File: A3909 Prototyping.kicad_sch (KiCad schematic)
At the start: 0 parts

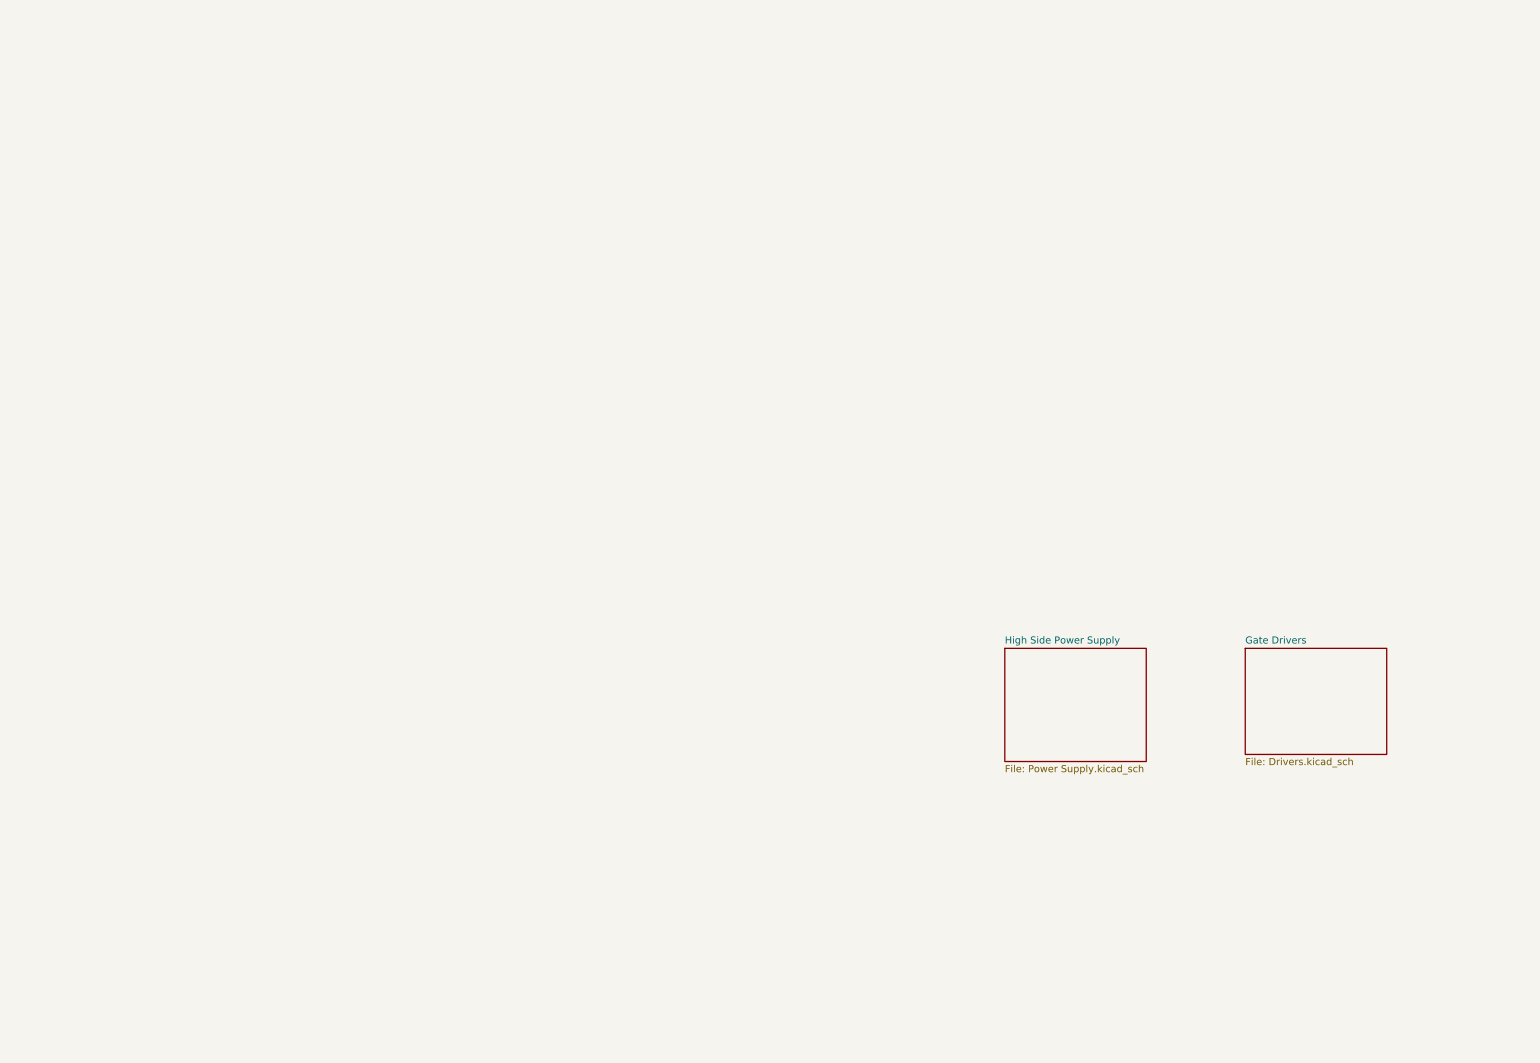
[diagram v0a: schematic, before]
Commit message: Final design Rev 1.0
Finalized design rev 1.0. Ordered from JLCPB
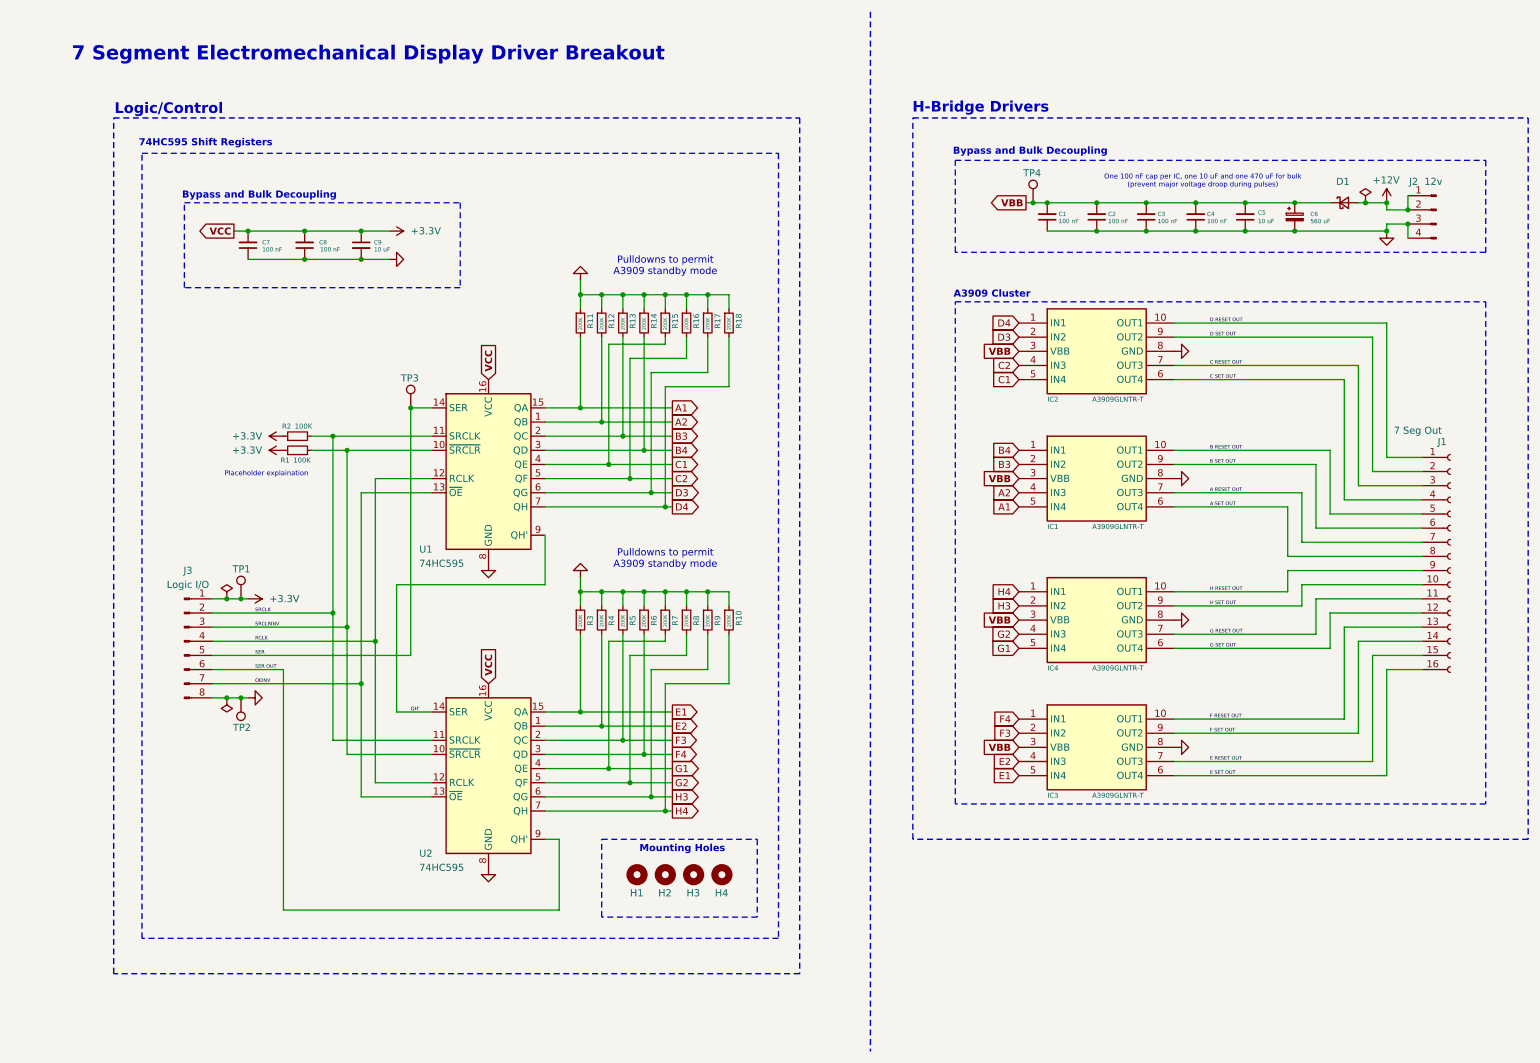
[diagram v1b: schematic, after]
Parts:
- added C1, C2, C3, C4, C7, C8: 100 nF, Capacitor_SMD:C_0402_1005Metric, symbol Device:C_Small
- added C5, C9: 10 uF, Capacitor_SMD:C_1206_3216Metric, symbol Device:C_Small
- added C6: 560 uF, Capacitor_SMD:C_Elec_10x10.2, symbol Device:C_Polarized_Small
- added D1: D_Schottky_Small, Diode_SMD:D_SMB, symbol Device:D_Schottky_Small
- added H1, H2, H3, H4: MountingHole, MountingHole:MountingHole_2.2mm_M2, symbol Mechanical:MountingHole
- added IC1, IC2, IC3, IC4: A3909GLNTR-T, KiCad:SOP100P600X175-10N, symbol A3909GLNTR-T:A3909GLNTR-T
- added J1: 7 Seg Out, Connector_PinHeader_2.54mm:PinHeader_1x16_P2.54mm_Vertical, symbol Connector:Conn_01x16_Socket
- added J2: 12v, Connector_PinHeader_2.54mm:PinHeader_1x04_P2.54mm_Vertical, symbol Connector:Conn_01x04_Pin
- added J3: Logic I/O, Connector_PinHeader_2.54mm:PinHeader_1x08_P2.54mm_Vertical, symbol Connector:Conn_01x08_Pin
- added R1, R2: 100K, Resistor_SMD:R_0402_1005Metric, symbol Device:R_Small
- added R10, R11, R12, R13, R14, R15, R16, R17, R18, R3, R4, R5, R6, R7, R8, R9: 200K, Resistor_SMD:R_0402_1005Metric, symbol Device:R_Small
- added TP1: 3.3v, TestPoint:TestPoint_Pad_D1.5mm, symbol Connector:TestPoint
- added TP2: GND, TestPoint:TestPoint_Pad_D1.5mm, symbol Connector:TestPoint
- added TP3: SER, TestPoint:TestPoint_Pad_D1.5mm, symbol Connector:TestPoint
- added TP4: 12v, TestPoint:TestPoint_Pad_D1.5mm, symbol Connector:TestPoint
- added U1, U2: 74HC595, Package_SO:SOIC-16_3.9x9.9mm_P1.27mm, symbol 74xx:74HC595
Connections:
- new net +12V: D1.2 (A), J2.1 (Pin_1), J2.2 (Pin_2)
- new net +3.3V: C7.2, C8.2, C9.1, J3.1 (Pin_1), R1.1, R2.1, TP1.1, U1.16 (VCC), U2.16 (VCC)
- new net A RESET OUT: IC1.7 (OUT3), J1.7 (Pin_7)
- new net A SET OUT: IC1.6 (OUT4), J1.8 (Pin_8)
- new net A1: IC1.5 (IN4), R11.2, U1.15 (QA)
- new net A2: IC1.4 (IN3), R12.2, U1.1 (QB)
- new net B RESET OUT: IC1.10 (OUT1), J1.5 (Pin_5)
- new net B SET OUT: IC1.9 (OUT2), J1.6 (Pin_6)
- new net B3: IC1.2 (IN2), R13.2, U1.2 (QC)
- new net B4: IC1.1 (IN1), R14.2, U1.3 (QD)
- new net C RESET OUT: IC2.7 (OUT3), J1.3 (Pin_3)
- new net C SET OUT: IC2.6 (OUT4), J1.4 (Pin_4)
- new net C1: IC2.5 (IN4), R15.2, U1.4 (QE)
- new net C2: IC2.4 (IN3), R16.2, U1.5 (QF)
- new net D RESET OUT: IC2.10 (OUT1), J1.1 (Pin_1)
- new net D SET OUT: IC2.9 (OUT2), J1.2 (Pin_2)
- new net D3: IC2.2 (IN2), R17.2, U1.6 (QG)
- new net D4: IC2.1 (IN1), R18.2, U1.7 (QH)
- new net E RESET OUT: IC3.7 (OUT3), J1.15 (Pin_15)
- new net E SET OUT: IC3.6 (OUT4), J1.16 (Pin_16)
- new net E1: IC3.5 (IN4), R3.2, U2.15 (QA)
- new net E2: IC3.4 (IN3), R4.2, U2.1 (QB)
- new net F RESET OUT: IC3.10 (OUT1), J1.13 (Pin_13)
- new net F SET OUT: IC3.9 (OUT2), J1.14 (Pin_14)
- new net F3: IC3.2 (IN2), R5.2, U2.2 (QC)
- new net F4: IC3.1 (IN1), R6.2, U2.3 (QD)
- new net G RESET OUT: IC4.7 (OUT3), J1.11 (Pin_11)
- new net G SET OUT: IC4.6 (OUT4), J1.12 (Pin_12)
- new net G1: IC4.5 (IN4), R7.2, U2.4 (QE)
- new net G2: IC4.4 (IN3), R8.2, U2.5 (QF)
- new net GND: C1.1, C2.1, C3.1, C4.1, C5.1, C6.2, C7.1, C8.1, C9.2, IC1.8 (GND), IC2.8 (GND), IC3.8 (GND), IC4.8 (GND), J2.3 (Pin_3), J2.4 (Pin_4), J3.8 (Pin_8), R10.1, R11.1, R12.1, R13.1, R14.1, R15.1, R16.1, R17.1, R18.1, R3.1, R4.1, R5.1, R6.1, R7.1, R8.1, R9.1, TP2.1, U1.8 (GND), U2.8 (GND)
- new net H RESET OUT: IC4.10 (OUT1), J1.9 (Pin_9)
- new net H SET OUT: IC4.9 (OUT2), J1.10 (Pin_10)
- new net H3: IC4.2 (IN2), R9.2, U2.6 (QG)
- new net H4: IC4.1 (IN1), R10.2, U2.7 (QH)
- new net OEINV: J3.7 (Pin_7), U1.13 (~{OE}), U2.13 (~{OE})
- new net QH': U1.9 (QH'), U2.14 (SER)
- new net RCLK: J3.4 (Pin_4), U1.12 (RCLK), U2.12 (RCLK)
- new net SER: J3.5 (Pin_5), TP3.1, U1.14 (SER)
- new net SER OUT: J3.6 (Pin_6), U2.9 (QH')
- new net SRCLK: J3.2 (Pin_2), R2.2, U1.11 (SRCLK), U2.11 (SRCLK)
- new net SRCLRINV: J3.3 (Pin_3), R1.2, U1.10 (~{SRCLR}), U2.10 (~{SRCLR})
- new net VBB: C1.2, C2.2, C3.2, C4.2, C5.2, C6.1, D1.1 (K), IC1.3 (VBB), IC2.3 (VBB), IC3.3 (VBB), IC4.3 (VBB), TP4.1
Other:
- removed sheet Gate Drivers
- removed sheet High Side Power Supply
- note added: "7 Segment Electromechanical Display Driver Breakout"
- note added: "74HC595 Shift Registers"
- note added: "A3909 Cluster"
- note added: "Bypass and Bulk Decoupling"
- note added: "H-Bridge Drivers"
- note added: "Logic/Control"
- note added: "Mounting Holes"
- note added: "One 100 nF cap per IC, one 10 uF and one 470 uF for bulk (prevent major voltage droop during pulses)"
- note added: "Placeholder explaination"
- note added: "Pulldowns to permit A3909 standby mode"
